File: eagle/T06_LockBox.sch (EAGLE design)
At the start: 30 parts, among them T1 2N3904, T2 2N3904, T3 2N3904

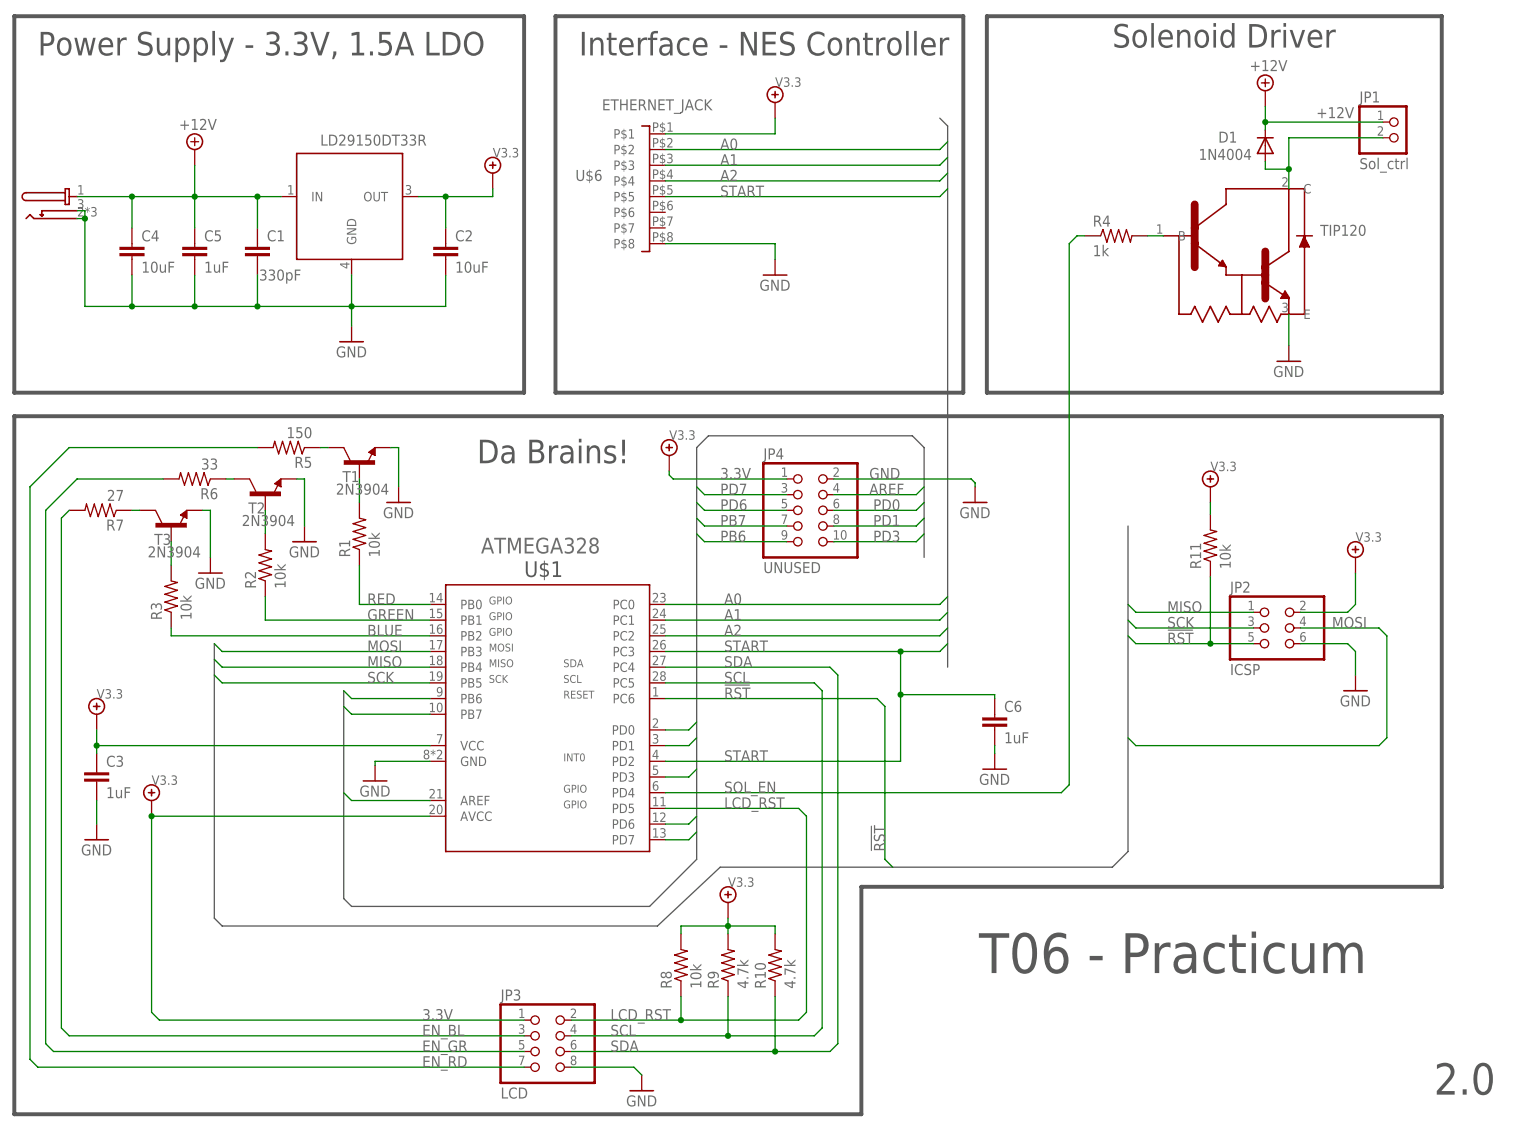
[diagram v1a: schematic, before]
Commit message: Increased drill size from .76mm to .9mm on the ethernet jack, this should provide enough space for pin diameter variations.
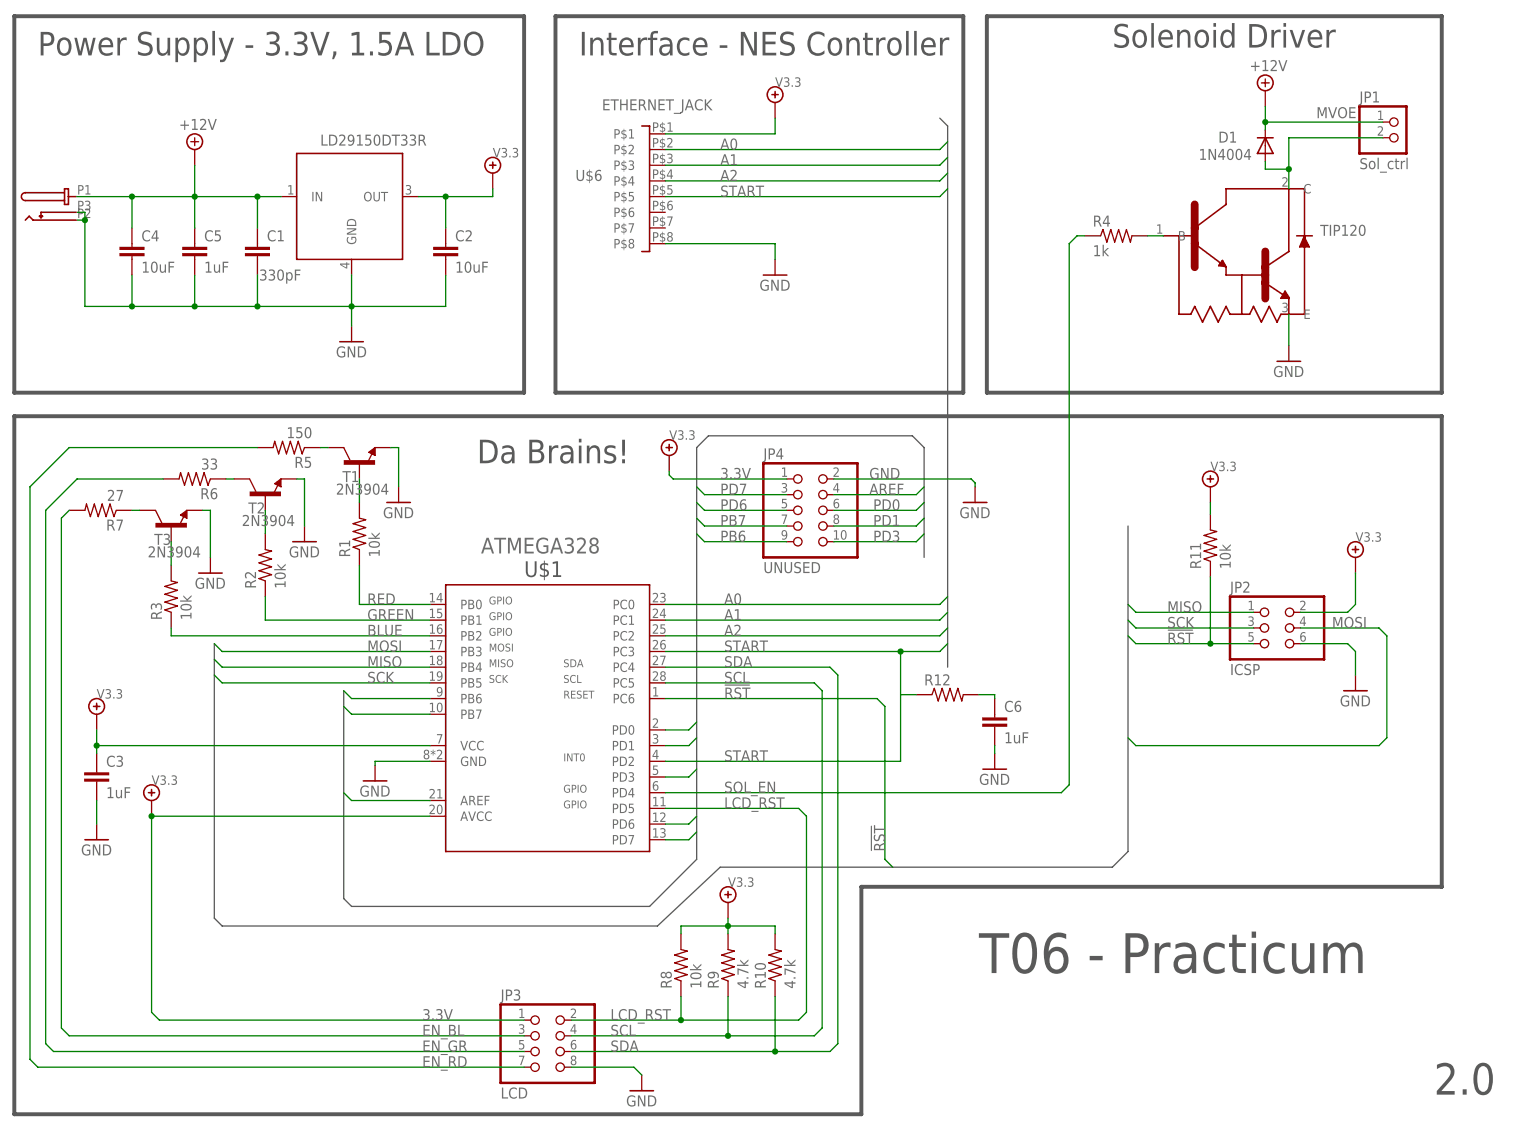
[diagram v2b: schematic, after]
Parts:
- added R12: (no value), T06_Lockbox:R-US_M0805
- U$3: value PJ_075DH -> PJ-102A; device T06_Lockbox:PJ_075DH -> T06_Lockbox:PJ-102A
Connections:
- net +12V renamed MVOE
- new net N$3: C6.1, R12.2
- net START: now also R12.1; no longer C6.1
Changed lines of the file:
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@@
 <setting verticaltext="up"/>
 </settings>
-<grid distance="0.025" unitdist="inch" unit="inch" style="lines" multiple="1" display="yes" altdistance="0.01" altunitdist="inch" altunit="inch"/>
+<grid distance="0.1" unitdist="inch" unit="inch" style="lines" multiple="1" display="no" altdistance="0.01" altunitdist="inch" altunit="inch"/>
 <layers>
 <layer number="1" name="Top" color="4" fill="1" visible="no" active="no"/>
@@
 <part name="FRAME1" library="T06_Lockbox" deviceset="FRAME-LETTER" device=""/>
 <part name="U$2" library="T06_Lockbox" deviceset="LD29150" device="" technology="DT33R"/>
-<part name="U$3" library="T06_Lockbox" deviceset="PJ_075" device="" technology="DH"/>
 <part name="GND1" library="T06_Lockbox" deviceset="GND" device=""/>
 <part name="V1" library="T06_Lockbox" deviceset="V3.3" device=""/>
@@
 <part name="R11" library="T06_Lockbox" deviceset="R-US_" device="M0805" value="10k"/>
 <part name="V8" library="T06_Lockbox" deviceset="V3.3" device=""/>
+<part name="U$3" library="T06_Lockbox" deviceset="PJ-102A" device=""/>
+<part name="R12" library="T06_Lockbox" deviceset="R-US_" device="M0805"/>
 </parts>
 <sheets>
@@
 <instance part="FRAME1" gate="G$2" x="147.32" y="0"/>
 <instance part="U$2" gate="G$1" x="57.15" y="149.86"/>
-<instance part="U$3" gate="G$1" x="14.605" y="150.495"/>
 <instance part="GND1" gate="1" x="60.96" y="127.635"/>
 <instance part="V1" gate="G1" x="83.82" y="154.94"/>
@@
 <instance part="R11" gate="G$1" x="200.025" y="94.615" rot="R90"/>
 <instance part="V8" gate="G1" x="200.025" y="104.14"/>
+<instance part="U$3" gate="G$1" x="13.97" y="151.13"/>
+<instance part="R12" gate="G$1" x="157.48" y="70.485"/>
 </instances>
 <busses>
@@
 <wire x1="35.56" y1="138.43" x2="35.56" y2="133.35" width="0.1524" layer="91"/>
 <junction x="35.56" y="133.35"/>
-<wire x1="17.78" y1="147.574" x2="17.78" y2="133.35" width="0.1524" layer="91"/>
 <wire x1="17.78" y1="133.35" x2="25.4" y2="133.35" width="0.1524" layer="91"/>
 <junction x="25.4" y="133.35"/>
+<wire x1="17.78" y1="133.35" x2="17.78" y2="147.32" width="0.1524" layer="91"/>
 <pinref part="U$3" gate="G$1" pin="GND@2"/>
-<wire x1="17.78" y1="147.574" x2="16.51" y2="147.574" width="0.1524" layer="91"/>
-<wire x1="17.78" y1="147.574" x2="17.78" y2="148.844" width="0.1524" layer="91"/>
-<junction x="17.78" y="147.574"/>
+<wire x1="17.78" y1="147.32" x2="16.51" y2="147.32" width="0.1524" layer="91"/>
+<junction x="17.78" y="147.32"/>
+<wire x1="17.78" y1="147.32" x2="17.78" y2="148.59" width="0.1524" layer="91"/>
 <pinref part="U$3" gate="G$1" pin="GND@1"/>
-<wire x1="17.78" y1="148.844" x2="16.51" y2="148.844" width="0.1524" layer="91"/>
+<wire x1="17.78" y1="148.59" x2="16.51" y2="148.59" width="0.1524" layer="91"/>
 </segment>
 <segment>
@@
 <label x="121.285" y="77.47" size="1.778" layer="95"/>
 <wire x1="149.86" y1="77.47" x2="111.76" y2="77.47" width="0.1524" layer="91"/>
+<pinref part="U$1" gate="G$1" pin="PD2"/>
 <wire x1="149.86" y1="77.47" x2="149.86" y2="70.485" width="0.1524" layer="91"/>
-<pinref part="U$1" gate="G$1" pin="PD2"/>
 <wire x1="149.86" y1="70.485" x2="149.86" y2="59.69" width="0.1524" layer="91"/>
 <wire x1="149.86" y1="59.69" x2="111.76" y2="59.69" width="0.1524" layer="91"/>
-<pinref part="C6" gate="G$1" pin="1"/>
-<wire x1="149.86" y1="70.485" x2="165.1" y2="70.485" width="0.1524" layer="91"/>
-<wire x1="165.1" y1="70.485" x2="165.1" y2="69.85" width="0.1524" layer="91"/>
-<junction x="149.86" y="70.485"/>
 <label x="121.285" y="59.69" size="1.778" layer="95"/>
 <wire x1="156.21" y1="77.47" x2="149.86" y2="77.47" width="0.1524" layer="91"/>
 <junction x="149.86" y="77.47"/>
-</segment>
-</net>
-<net name="+12V" class="0">
+<pinref part="R12" gate="G$1" pin="1"/>
+<wire x1="152.4" y1="70.485" x2="149.86" y2="70.485" width="0.1524" layer="91"/>
+</segment>
+</net>
+<net name="MVOE" class="0">
 <segment>
 <pinref part="SUPPLY2" gate="+12V" pin="+12V"/>
@@
 <pinref part="U$2" gate="G$1" pin="IN"/>
 <wire x1="49.53" y1="151.13" x2="45.72" y2="151.13" width="0.1524" layer="91"/>
-<pinref part="U$3" gate="G$1" pin="PWR"/>
 <pinref part="C1" gate="G$1" pin="1"/>
 <wire x1="45.72" y1="151.13" x2="35.56" y2="151.13" width="0.1524" layer="91"/>
@@
 <wire x1="35.56" y1="156.21" x2="35.56" y2="151.13" width="0.1524" layer="91"/>
 <pinref part="SUPPLY1" gate="+12V" pin="+12V"/>
+<pinref part="U$3" gate="G$1" pin="PWR"/>
 </segment>
 </net>
@@
 </segment>
 </net>
+<net name="N$3" class="0">
+<segment>
+<pinref part="C6" gate="G$1" pin="1"/>
+<wire x1="165.1" y1="70.485" x2="165.1" y2="69.85" width="0.1524" layer="91"/>
+<pinref part="R12" gate="G$1" pin="2"/>
+<wire x1="162.56" y1="70.485" x2="165.1" y2="70.485" width="0.1524" layer="91"/>
+</segment>
+</net>

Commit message: Added cap to VCC next to atmel chip, increased 3.3V trace width, text size issue was not related to our file but Andrews eagle that always displayed vector font
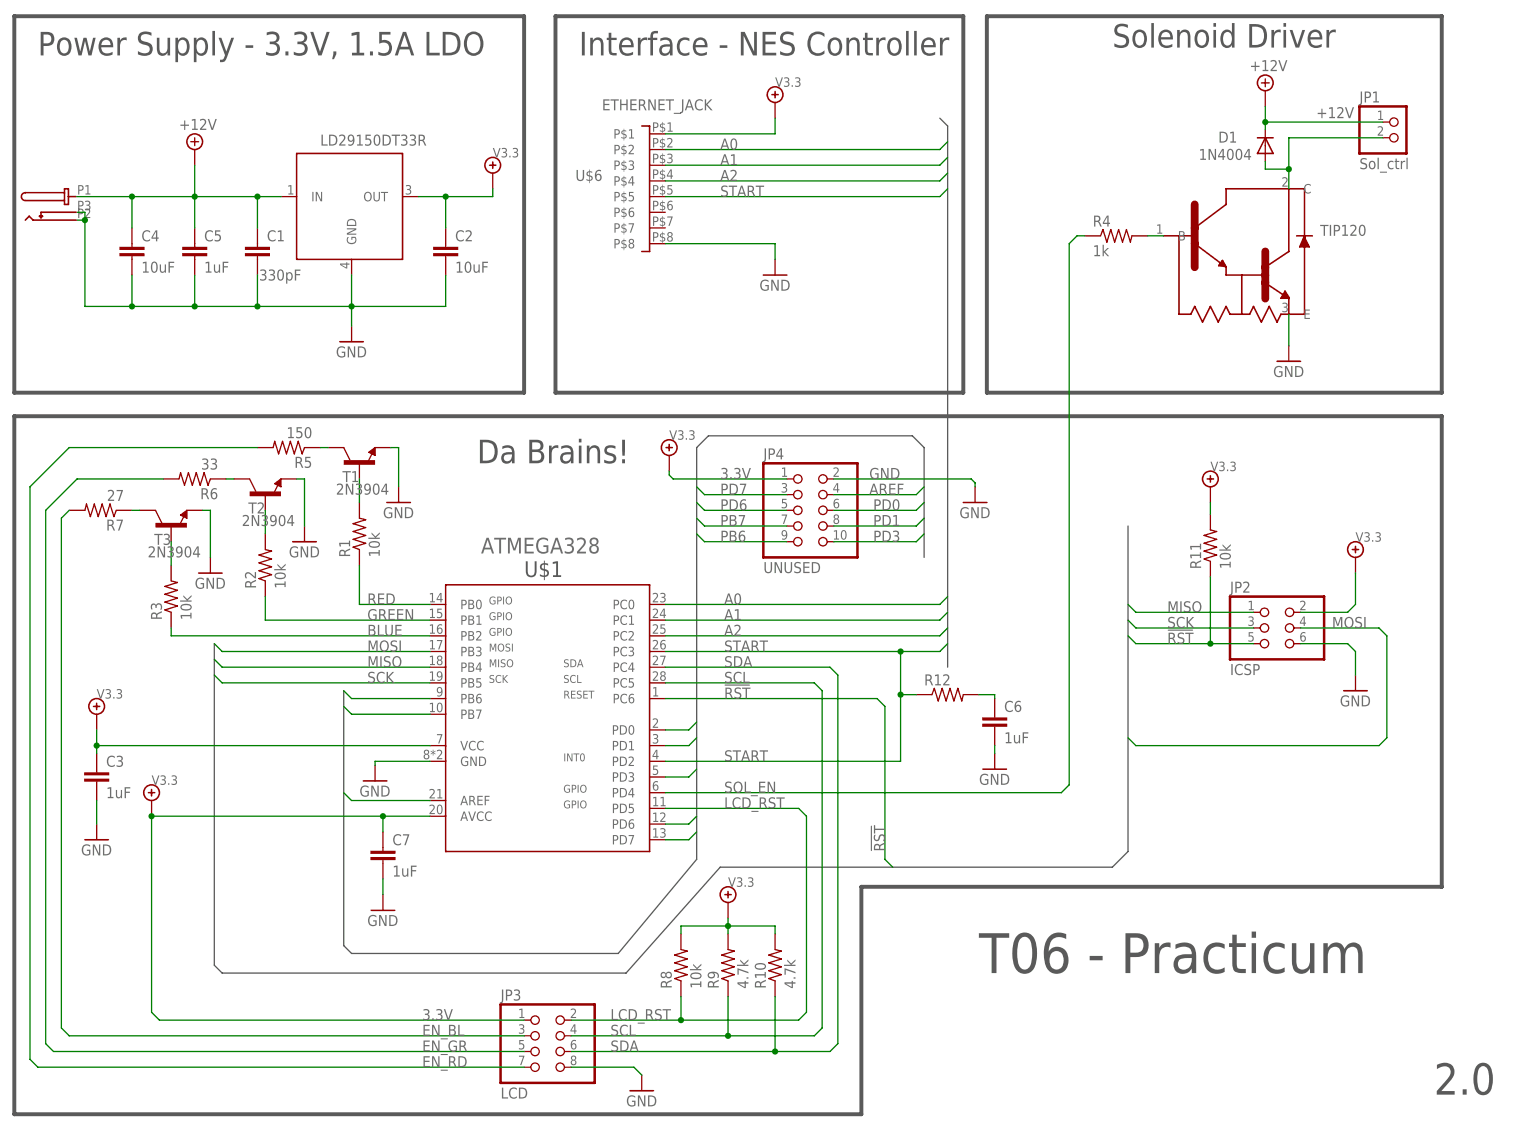
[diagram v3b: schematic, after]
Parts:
- added C7: 1uF, T06_Lockbox:C
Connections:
- net MVOE renamed +12V
- net 3.3V: now also C7.1
- net GND: now also C7.2
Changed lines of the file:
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@@
 <setting verticaltext="up"/>
 </settings>
-<grid distance="0.1" unitdist="inch" unit="inch" style="lines" multiple="1" display="no" altdistance="0.01" altunitdist="inch" altunit="inch"/>
+<grid distance="0.1" unitdist="inch" unit="inch" style="lines" multiple="1" display="yes" altdistance="0.01" altunitdist="inch" altunit="inch"/>
 <layers>
 <layer number="1" name="Top" color="4" fill="1" visible="no" active="no"/>
@@
 <part name="U$3" library="T06_Lockbox" deviceset="PJ-102A" device=""/>
 <part name="R12" library="T06_Lockbox" deviceset="R-US_" device="M0805"/>
+<part name="C7" library="T06_Lockbox" deviceset="C" device="" value="1uF"/>
+<part name="GND13" library="T06_Lockbox" deviceset="GND" device=""/>
 </parts>
 <sheets>
@@
 <instance part="U$3" gate="G$1" x="13.97" y="151.13"/>
 <instance part="R12" gate="G$1" x="157.48" y="70.485"/>
+<instance part="C7" gate="G$1" x="66.04" y="45.72"/>
+<instance part="GND13" gate="1" x="66.04" y="35.56"/>
 </instances>
 <busses>
@@
 <bus name="ICSP_BUS:MISO,MOSI,!RST,SCK">
 <segment>
-<wire x1="38.735" y1="78.74" x2="38.735" y2="34.29" width="0.762" layer="92"/>
-<wire x1="38.735" y1="34.29" x2="40.005" y2="33.02" width="0.762" layer="92"/>
-<wire x1="40.005" y1="33.02" x2="110.49" y2="33.02" width="0.762" layer="92"/>
-<wire x1="110.49" y1="33.02" x2="120.65" y2="42.545" width="0.762" layer="92"/>
+<wire x1="38.735" y1="78.74" x2="38.735" y2="26.67" width="0.762" layer="92"/>
+<wire x1="38.735" y1="26.67" x2="40.005" y2="25.4" width="0.762" layer="92"/>
+<wire x1="40.005" y1="25.4" x2="105.41" y2="25.4" width="0.762" layer="92"/>
+<wire x1="105.41" y1="25.4" x2="120.65" y2="42.545" width="0.762" layer="92"/>
 <wire x1="120.65" y1="42.545" x2="184.15" y2="42.545" width="0.762" layer="92"/>
 <wire x1="184.15" y1="42.545" x2="186.69" y2="45.085" width="0.762" layer="92"/>
@@
 <bus name="UNUSED:AREF,PB6,PB7,PD0,PD1,PD3,PD6,PD7">
 <segment>
-<wire x1="59.69" y1="71.12" x2="59.69" y2="37.465" width="0.762" layer="92"/>
-<wire x1="59.69" y1="37.465" x2="60.96" y2="36.195" width="0.762" layer="92"/>
-<wire x1="60.96" y1="36.195" x2="109.22" y2="36.195" width="0.762" layer="92"/>
-<wire x1="109.22" y1="36.195" x2="116.84" y2="43.815" width="0.762" layer="92"/>
+<wire x1="59.69" y1="71.12" x2="59.69" y2="29.845" width="0.762" layer="92"/>
+<wire x1="59.69" y1="29.845" x2="60.96" y2="28.575" width="0.762" layer="92"/>
+<wire x1="60.96" y1="28.575" x2="104.14" y2="28.575" width="0.762" layer="92"/>
+<wire x1="104.14" y1="28.575" x2="116.84" y2="43.815" width="0.762" layer="92"/>
 <wire x1="116.84" y1="43.815" x2="116.84" y2="110.49" width="0.762" layer="92"/>
 <wire x1="116.84" y1="110.49" x2="118.745" y2="112.395" width="0.762" layer="92"/>
@@
 <label x="144.78" y="105.41" size="1.778" layer="95"/>
 </segment>
+<segment>
+<pinref part="C7" gate="G$1" pin="2"/>
+<wire x1="66.04" y1="40.64" x2="66.04" y2="38.1" width="0.1524" layer="91"/>
+<pinref part="GND13" gate="1" pin="GND"/>
+</segment>
 </net>
 <net name="SDA" class="0">
@@
 <pinref part="R12" gate="G$1" pin="1"/>
 <wire x1="152.4" y1="70.485" x2="149.86" y2="70.485" width="0.1524" layer="91"/>
-</segment>
-</net>
-<net name="MVOE" class="0">
+<junction x="149.86" y="70.485"/>
+</segment>
+</net>
+<net name="+12V" class="0">
 <segment>
 <pinref part="SUPPLY2" gate="+12V" pin="+12V"/>
@@
 <segment>
 <pinref part="U$1" gate="G$1" pin="AVCC"/>
-<wire x1="73.66" y1="50.8" x2="28.575" y2="50.8" width="0.1524" layer="91"/>
+<wire x1="73.66" y1="50.8" x2="66.04" y2="50.8" width="0.1524" layer="91"/>
+<wire x1="66.04" y1="50.8" x2="28.575" y2="50.8" width="0.1524" layer="91"/>
 <wire x1="28.575" y1="50.8" x2="28.575" y2="19.05" width="0.1524" layer="91"/>
 <wire x1="28.575" y1="19.05" x2="29.845" y2="17.78" width="0.1524" layer="91"/>
@@
 <pinref part="V5" gate="G1" pin="3.3V"/>
 <junction x="28.575" y="50.8"/>
-</segment>
-<segment>
+<pinref part="C7" gate="G$1" pin="1"/>
+<wire x1="66.04" y1="50.8" x2="66.04" y2="48.26" width="0.1524" layer="91"/>
+<junction x="66.04" y="50.8"/>
+</segment>
+<segment>
